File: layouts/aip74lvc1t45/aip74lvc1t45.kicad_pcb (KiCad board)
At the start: 2 copper layers, 3 parts

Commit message: refactor jlink connector, make stick prety
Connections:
- net -hv-0 renamed power_a-VCC
- net -hv-1 renamed power_b-VCC
- net gnd renamed GND
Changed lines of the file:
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@@
     )
     (net 0 "")
-    (net 1 "-hv-1")
+    (net 1 "power_b-VCC")
     (net 2 "A")
     (net 3 "B")
     (net 4 "DIR")
-    (net 5 "-hv-0")
-    (net 6 "gnd")
+    (net 5 "power_a-VCC")
+    (net 6 "GND")
     (footprint "Wuxi_I_core_Elec_AiP74LVC1T45GB236_TR:SOT-23-6_L2.9-W1.6-P0.95-LS2.8-BL"
         (layer "F.Cu")
@@
             (size 0.53 1.07)
             (layers "F.Cu" "F.Mask" "F.Paste")
-            (net 5 "-hv-0")
+            (net 5 "power_a-VCC")
         )
         (pad "2" smd rect
@@
             (size 0.53 1.07)
             (layers "F.Cu" "F.Mask" "F.Paste")
-            (net 6 "gnd")
+            (net 6 "GND")
         )
         (pad "3" smd rect
@@
             (size 0.53 1.07)
             (layers "F.Cu" "F.Mask" "F.Paste")
-            (net 1 "-hv-1")
+            (net 1 "power_b-VCC")
         )
         (embedded_fonts no)
@@
             (size 0.79 0.54)
             (layers "F.Cu" "F.Mask" "F.Paste")
-            (net 5 "-hv-0")
+            (net 5 "power_a-VCC")
         )
         (pad "2" smd rect
@@
             (size 0.79 0.54)
             (layers "F.Cu" "F.Mask" "F.Paste")
-            (net 6 "gnd")
+            (net 6 "GND")
         )
         (embedded_fonts no)
@@
             (size 0.79 0.54)
             (layers "F.Cu" "F.Mask" "F.Paste")
-            (net 1 "-hv-1")
+            (net 1 "power_b-VCC")
         )
         (pad "2" smd rect
@@
             (size 0.79 0.54)
             (layers "F.Cu" "F.Mask" "F.Paste")
-            (net 6 "gnd")
+            (net 6 "GND")
         )
         (embedded_fonts no)

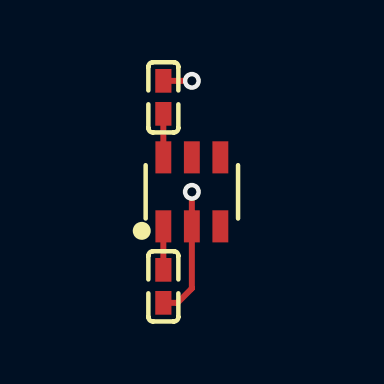
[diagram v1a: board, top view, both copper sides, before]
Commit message: refactor debug-connectors, fix issues in layout and connections
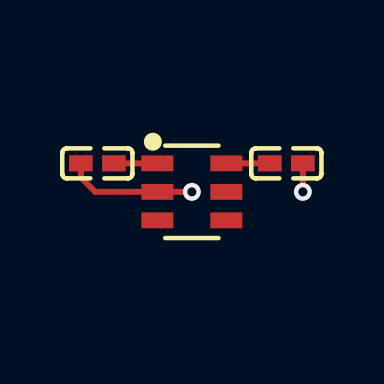
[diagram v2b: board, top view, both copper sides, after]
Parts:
- moved C1 4.65 mm to (-3.15, -0.95), turned to 180 degrees
- moved C2 4.65 mm to (3.15, -0.95), turned to 0 degrees
- turned U1 to -90 degrees

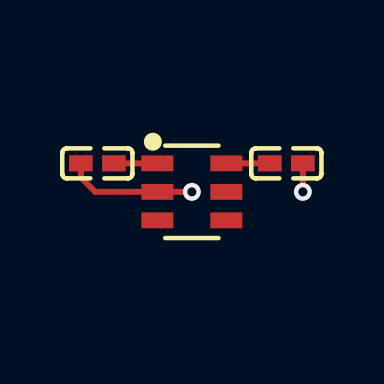
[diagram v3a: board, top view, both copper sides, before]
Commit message: fix swapped jlink connector pinout + update deps
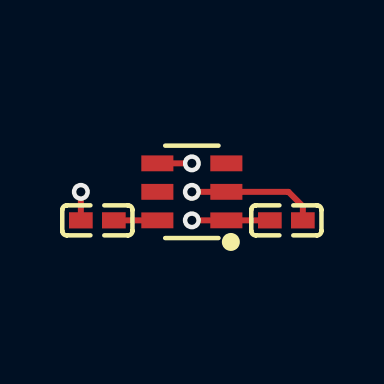
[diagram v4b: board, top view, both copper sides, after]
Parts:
- moved C2 6.58 mm to (-3.15, 0.95), turned to 180 degrees
- moved C1 6.58 mm to (3.15, 0.95), turned to 0 degrees
- turned U1 to 90 degrees
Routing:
- net B: track 0.00 -> 1.15 mm, vias 0 -> 1
- net power_a-VCC: track 1.45 -> 2.60 mm, vias 0 -> 1
